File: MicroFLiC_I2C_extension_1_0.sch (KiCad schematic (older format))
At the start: 13 parts, among them P1 Header_1x14, P2 Socket_1x14, P3 8-188275-4, P4 Header_1x4, P5 Socket_1x4, P6 DB15-VGA, P7 RJ45, SW1 SW_PUSH, SW2 DIPS_04

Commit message: Final production board v1.0
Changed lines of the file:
@@
 EESchema Schematic File Version 2
+LIBS:MicroFLiC_I2C_extension_1_0-rescue
 LIBS:power
 LIBS:device
@@
 $EndComp
 Wire Wire Line
-	5250 2650 5250 3150
-Wire Wire Line
-	5350 2650 5350 3150
-Wire Wire Line
-	5450 2650 5450 3150
-Wire Wire Line
-	5550 2650 5550 3150
-Wire Wire Line
-	5250 3650 5250 3850
-Wire Wire Line
-	5350 3650 5350 3850
-Wire Wire Line
-	5450 3850 5450 3650
-Wire Wire Line
-	5550 3850 5550 3650
+	5250 2650 5250 3250
+Wire Wire Line
+	5350 2650 5350 3250
+Wire Wire Line
+	5450 2650 5450 3250
+Wire Wire Line
+	5550 2650 5550 3250
+Wire Wire Line
+	5250 3550 5250 3850
+Wire Wire Line
+	5350 3550 5350 3850
+Wire Wire Line
+	5450 3850 5450 3550
+Wire Wire Line
+	5550 3850 5550 3550
 Wire Wire Line
 	5250 3850 5550 3850

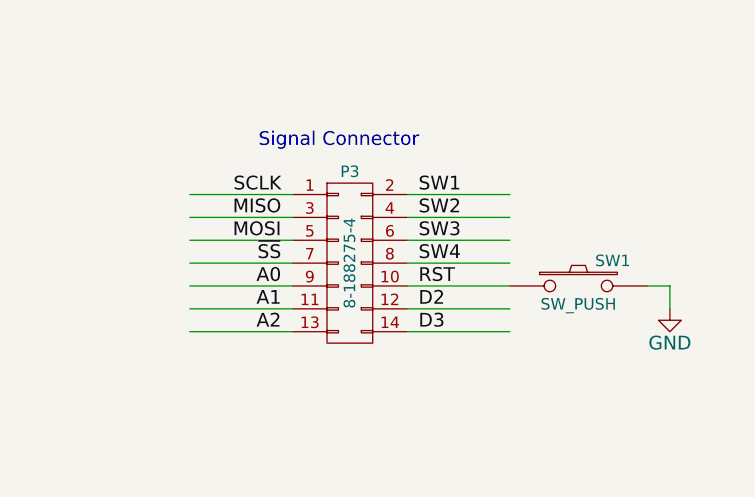
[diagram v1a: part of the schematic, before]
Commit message: Fixed part numbers
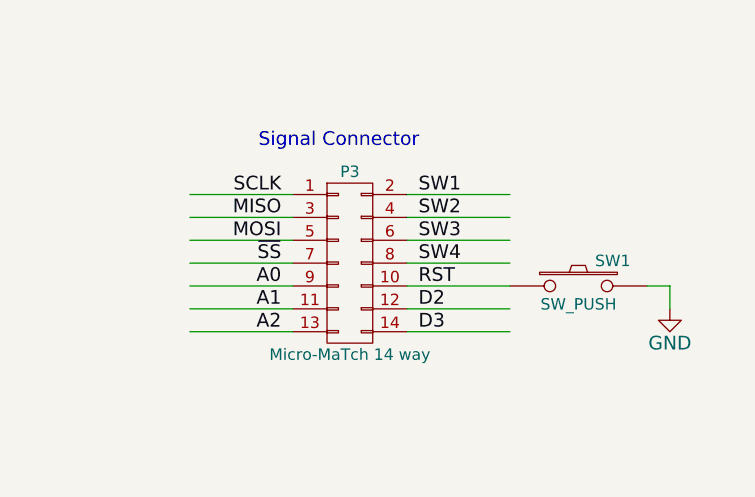
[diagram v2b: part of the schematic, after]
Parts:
- P1: Manufacturer Samtec -> Multicomp; Order Code 2010798 -> 1593421; Part Number HTSW-114-15-G-S -> MC34735
- P3: value 8-188275-4 -> Micro-MaTch 14 way
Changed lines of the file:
@@
 F 2 "Pin_Headers:Pin_Header_Straight_1x14" H 1300 1950 60  0001 C CNN
 F 3 "" H 1300 1950 60  0000 C CNN
-F 4 "HTSW-114-15-G-S" H 1300 1950 60  0001 C CNN "Part Number"
-F 5 "Samtec" H 1300 1950 60  0001 C CNN "Manufacturer"
-F 6 "2010798" H 1300 1950 60  0001 C CNN "Order Code"
+F 4 "MC34735" H 1300 1950 60  0001 C CNN "Part Number"
+F 5 "Multicomp" H 1300 1950 60  0001 C CNN "Manufacturer"
+F 6 "1593421" H 1300 1950 60  0001 C CNN "Order Code"
 	1    1300 1950
 	-1   0    0    -1
@@
 P 2600 4400
 F 0 "P3" H 2600 4800 50  0000 C CNN
-F 1 "8-188275-4" V 2600 4400 50  0000 C CNN
+F 1 "Micro-MaTch 14 way" H 2600 4000 50  0000 C CNN
 F 2 "jakub:1-188275-4" H 2600 3200 60  0001 C CNN
 F 3 "" H 2600 3200 60  0000 C CNN
